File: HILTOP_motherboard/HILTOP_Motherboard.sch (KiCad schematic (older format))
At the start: 216 parts, among them J1 BACKPLANE_PWR, J10 HDMI, J11 DISP_PWR, J12 DISPLAY_PORT, J14 VADJ_B, J15 VADJ_A, J16 SOFT_START_PWR, J17 PWR_LED, J18 USB_B, J19 Micro_SD_Card, J2 ATX_MOLEX_02X12, J20 CAMERA_PORT, J21 EXT_FAN, J22 BACKPLANE_LV_PWR, J23 EXT_FAN, J26 IO_EXP, J27 USB_A, J3 SATA, J4 USB_A_DOUBLE, J5 USB FRONT PANEL, J6 CAN, J7 RS485, J8 EXT_TEMP_MON, J9 RJ45-TRANS_SI-61001-F, U1 LM337BD2TG, U25 STM6719SFWB6F, U39 MCP23017, U42 24LC512

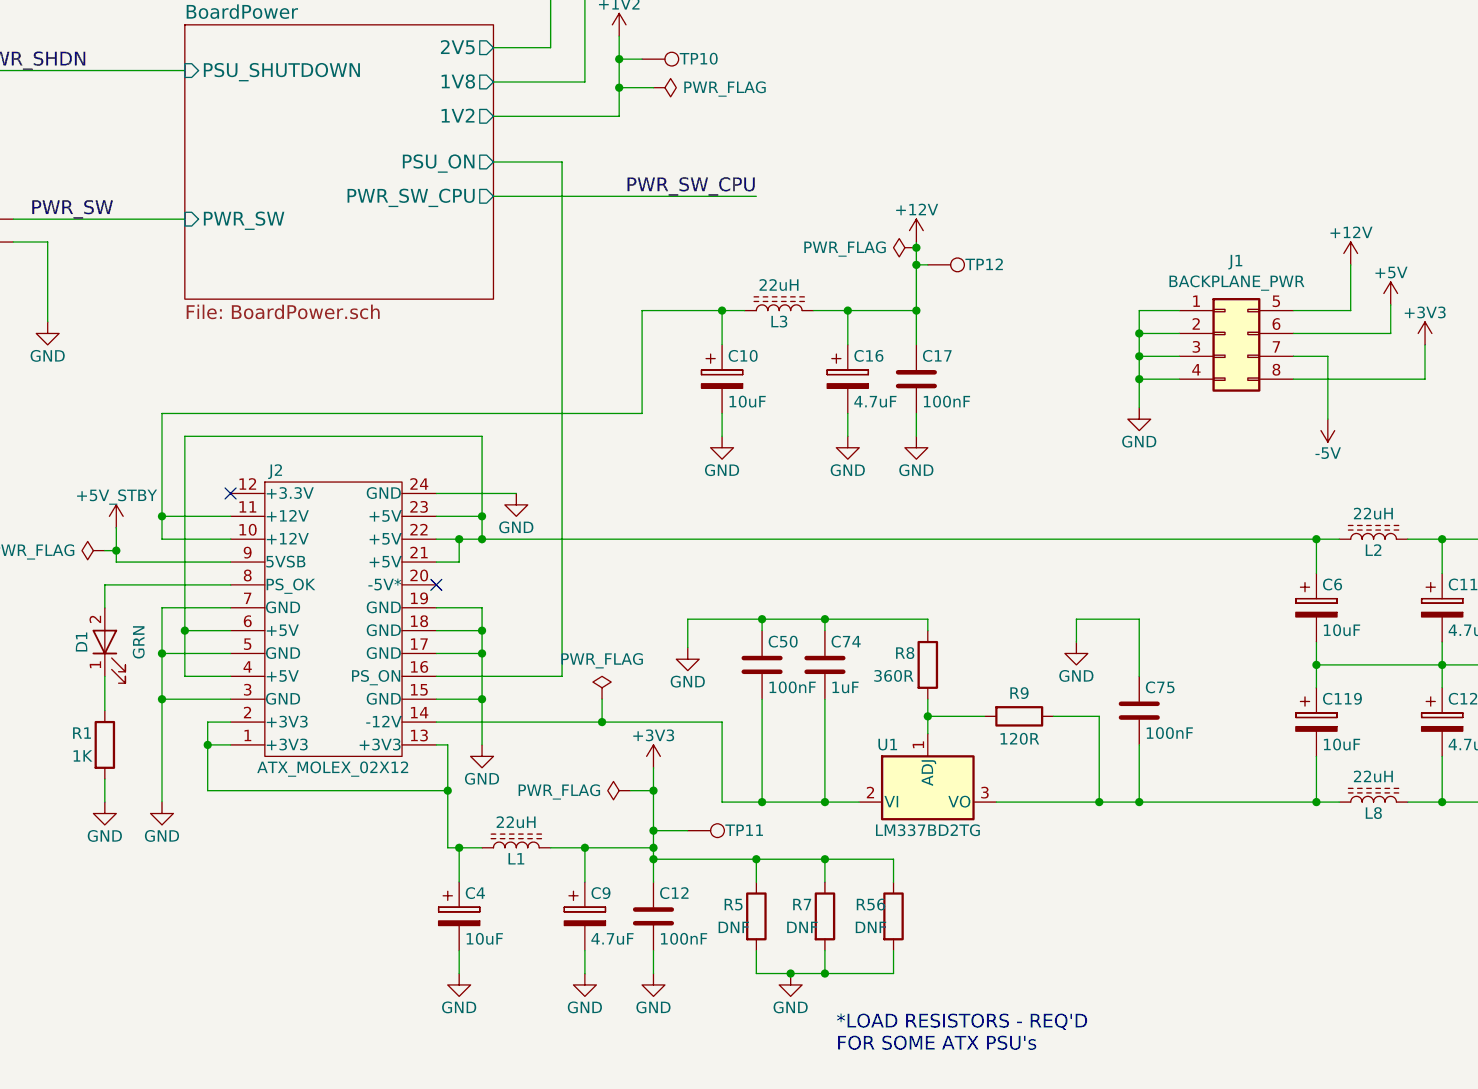
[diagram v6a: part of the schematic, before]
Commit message: Added TVS diodes on PSU inputs, update license details
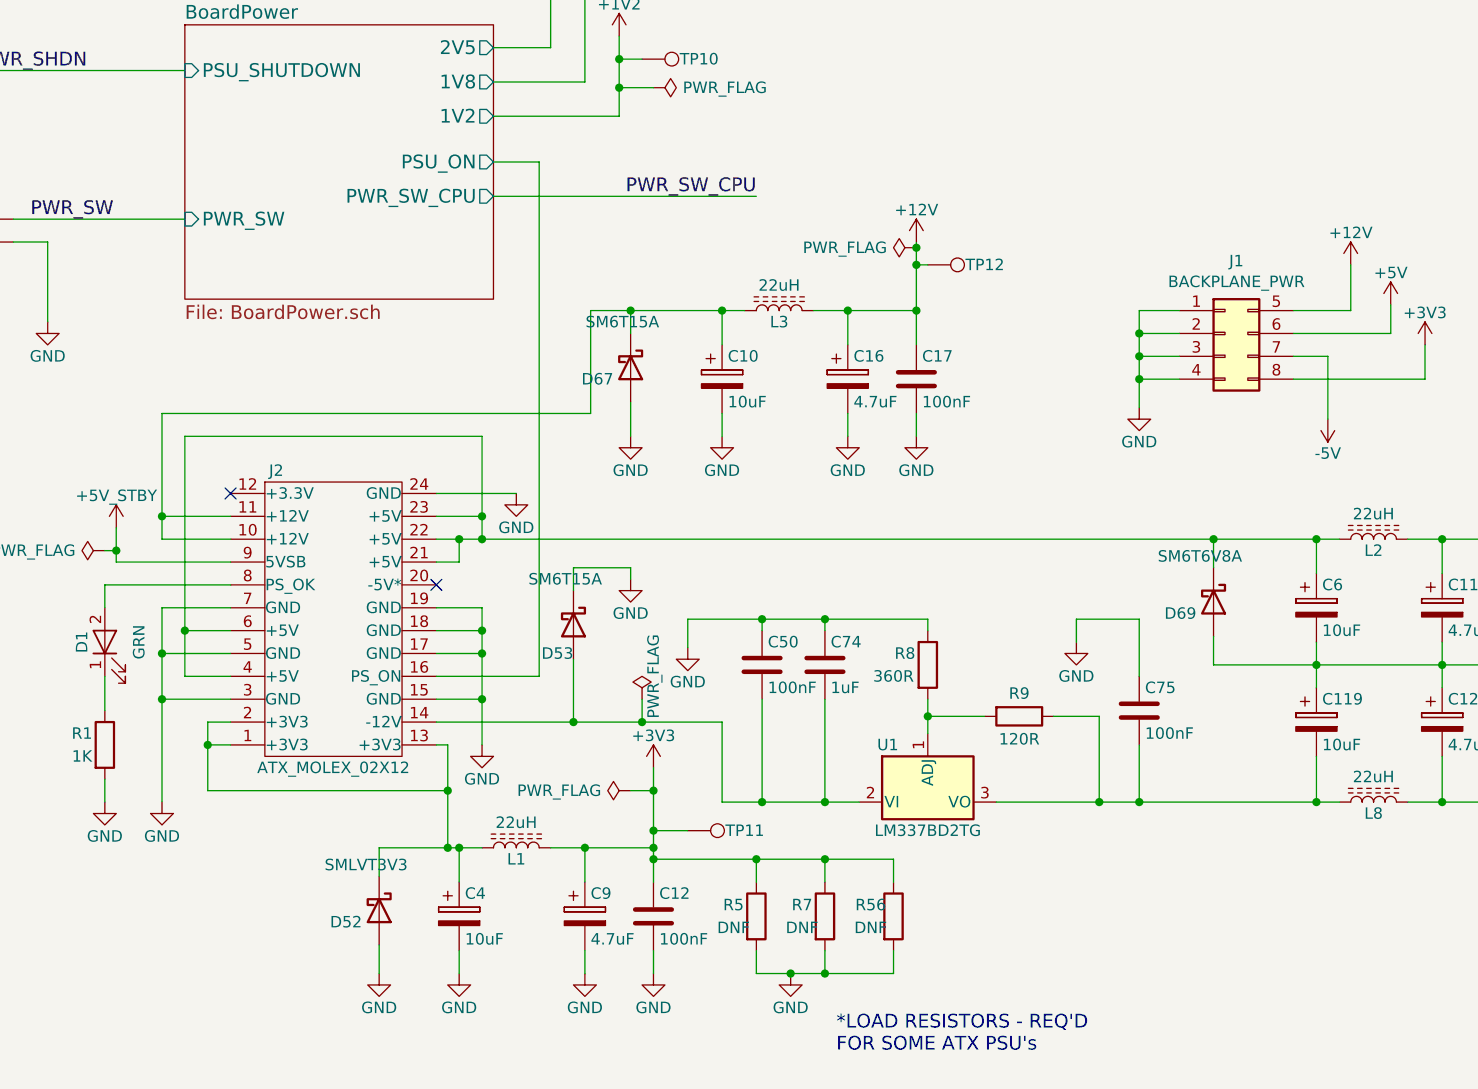
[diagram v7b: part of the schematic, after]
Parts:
- added D52: SMLVT3V3, Diode_SMD:D_SMB, symbol Device:D_Schottky
- added D53, D67: SM6T15A, Diode_SMD:D_SMB, symbol Device:D_Schottky
- added D69: SM6T6V8A, Diode_SMD:D_SMB, symbol Device:D_Schottky
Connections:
- net GND: now also D52.2 (A), D53.1 (K), D67.2 (A), D69.2 (A)
- net at C4.1, J2.1 (+3V3), J2.13 (+3V3)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: now also D52.1 (K)
- net at C6.1, J2.21 (+5V), J2.22 (+5V)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: now also D69.1 (K)
- net at C10.1, J2.10 (+12V), J2.11 (+12V)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: now also D67.1 (K)
- net at C50.2, C74.2, J2.14 (-12V)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: now also D53.2 (A)
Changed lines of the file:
@@
 	1800 13250 1800 13700
 Wire Wire Line
-	3900 13250 1800 13250
+	3675 13250 1800 13250
 Wire Wire Line
-	3900 12800 3900 13250
+	3675 12800 3675 13250
 Wire Wire Line
-	3900 12800 4250 12800
+	3675 12800 3850 12800
 Connection ~ 5100 12800
 Wire Wire Line
@@
 	3800 11600 3800 11700
 Wire Wire Line
-	3550 14400 3000 14400
+	3450 14400 3000 14400
 Wire Wire Line
-	3250 12150 3550 12150
+	3250 12150 3450 12150
 Wire Wire Line
 	1550 14000 2100 14000
@@
 	1    0    0    -1
 $EndComp
-Wire Wire Line
-	3200 13800 6850 13800
 $Comp
 L HILTOP_Motherboard-rescue:R-device R8
@@
 	4250 14950 4250 14600
 Wire Wire Line
-	4250 14600 3725 14600
+	4250 14600 3900 14600
 Wire Wire Line
 	5150 14500 5150 14575
@@
 L power:PWR_FLAG #FLG0129
 U 1 1 5E6340CA
-P 3725 14500
-F 0 "#FLG0129" H 3725 14575 50  0001 C CNN
-F 1 "PWR_FLAG" H 3725 14674 50  0000 C CNN
-F 2 "" H 3725 14500 50  0001 C CNN
-F 3 "" H 3725 14500 50  0001 C CNN
-	1    3725 14500
+P 3900 14500
+F 0 "#FLG0129" H 3900 14575 50  0001 C CNN
+F 1 "PWR_FLAG" V 3950 14600 50  0000 C CNN
+F 2 "" H 3900 14500 50  0001 C CNN
+F 3 "" H 3900 14500 50  0001 C CNN
+	1    3900 14500
 	1    0    0    -1
 $EndComp
 Wire Wire Line
-	3725 14500 3725 14600
-Connection ~ 3725 14600
-Wire Wire Line
-	3725 14600 3000 14600
+	3900 14500 3900 14600
+Connection ~ 3900 14600
 $Comp
 L power:PWR_FLAG #FLG0130
@@
 $EndSheet
 Wire Wire Line
-	3550 12150 3550 14400
-Wire Wire Line
 	3250 12300 4400 12300
 Text Label 4400 12300 2    60   ~ 0
@@
 Wire Wire Line
 	4525 8400 4650 8400
+$Comp
+L Device:D_Schottky D67
+U 1 1 60428387
+P 3850 13050
+F 0 "D67" V 3900 12975 50  0000 R CNN
+F 1 "SM6T15A" V 3650 13175 50  0000 R CNN
+F 2 "Diode_SMD:D_SMB" H 3850 13050 50  0001 C CNN
+F 3 "~" H 3850 13050 50  0001 C CNN
+	1    3850 13050
+	0    1    1    0
+$EndComp
+$Comp
+L power:GND #PWR0473
+U 1 1 6086D8C1
+P 3850 13350
+F 0 "#PWR0473" H 3850 13100 50  0001 C CNN
+F 1 "GND" H 3850 13200 50  0000 C CNN
+F 2 "" H 3850 13350 50  0000 C CNN
+F 3 "" H 3850 13350 50  0000 C CNN
+	1    3850 13350
+	1    0    0    -1
+$EndComp
+Wire Wire Line
+	3850 13200 3850 13350
+Wire Wire Line
+	3850 12900 3850 12800
+Connection ~ 3850 12800
+Wire Wire Line
+	3850 12800 4250 12800
+$Comp
+L Device:D_Schottky D69
+U 1 1 60C90533
+P 6400 14075
+F 0 "D69" V 6450 14000 50  0000 R CNN
+F 1 "SM6T6V8A" V 6200 14200 50  0000 R CNN
+F 2 "Diode_SMD:D_SMB" H 6400 14075 50  0001 C CNN
+F 3 "~" H 6400 14075 50  0001 C CNN
+	1    6400 14075
+	0    1    1    0
+$EndComp
+Wire Wire Line
+	6400 14225 6400 14350
+Wire Wire Line
+	6400 14350 6850 14350
+Wire Wire Line
+	6400 13925 6400 13800
+Connection ~ 6400 13800
+Wire Wire Line
+	6400 13800 6850 13800
+$Comp
+L Device:D_Schottky D53
+U 1 1 60F71958
+P 3600 14175
+F 0 "D53" V 3725 14175 50  0000 R CNN
+F 1 "SM6T15A" V 3400 14300 50  0000 R CNN
+F 2 "Diode_SMD:D_SMB" H 3600 14175 50  0001 C CNN
+F 3 "~" H 3600 14175 50  0001 C CNN
+	1    3600 14175
+	0    1    1    0
+$EndComp
+Wire Wire Line
+	3200 13800 6400 13800
+Wire Wire Line
+	3600 14325 3600 14600
+Wire Wire Line
+	3000 14600 3600 14600
+Connection ~ 3600 14600
+Wire Wire Line
+	3600 14600 3900 14600
+$Comp
+L power:GND #PWR0475
+U 1 1 6167D747
+P 3850 13975
+F 0 "#PWR0475" H 3850 13725 50  0001 C CNN
+F 1 "GND" H 3850 13825 50  0000 C CNN
+F 2 "" H 3850 13975 50  0000 C CNN
+F 3 "" H 3850 13975 50  0000 C CNN
+	1    3850 13975
+	1    0    0    -1
+$EndComp
+Wire Wire Line
+	3850 13975 3850 13925
+Wire Wire Line
+	3850 13925 3600 13925
+Wire Wire Line
+	3600 13925 3600 14025
+$Comp
+L Device:D_Schottky D52
+U 1 1 617EAE20
+P 2750 15425
+F 0 "D52" V 2800 15350 50  0000 R CNN
+F 1 "SMLVT3V3" V 2550 15550 50  0000 R CNN
+F 2 "Diode_SMD:D_SMB" H 2750 15425 50  0001 C CNN
+F 3 "~" H 2750 15425 50  0001 C CNN
+	1    2750 15425
+	0    1    1    0
+$EndComp
+Wire Wire Line
+	2750 15275 2750 15150
+Wire Wire Line
+	2750 15150 3050 15150
+Connection ~ 3050 15150
+$Comp
+L power:GND #PWR0476
+U 1 1 619536F3
+P 2750 15700
+F 0 "#PWR0476" H 2750 15450 50  0001 C CNN
+F 1 "GND" H 2750 15550 50  0000 C CNN
+F 2 "" H 2750 15700 50  0000 C CNN
+F 3 "" H 2750 15700 50  0000 C CNN
+	1    2750 15700
+	1    0    0    -1
+$EndComp
+Wire Wire Line
+	2750 15575 2750 15700
+Wire Wire Line
+	3450 12150 3450 14400
 $EndSCHEMATC

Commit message: changed silkscreen to revD and updated sheet information
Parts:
- D52, D53, D67, D69: symbol Device:D_Schottky -> HILTOP_Motherboard-rescue:D_Schottky-Device
- J10: symbol Devtank:HDMI -> HILTOP_Motherboard-rescue:HDMI-Devtank
- J2: symbol Devtank:ATX_MOLEX_02X12 -> HILTOP_Motherboard-rescue:ATX_MOLEX_02X12-Devtank
- J4: symbol Devtank:USB_A_DOUBLE -> HILTOP_Motherboard-rescue:USB_A_DOUBLE-Devtank
- J9: symbol Devtank:RJ45-TRANS_SI-61001-F -> HILTOP_Motherboard-rescue:RJ45-TRANS_SI-61001-F-Devtank
- U25: symbol Devtank:STM6719SFWB6F -> HILTOP_Motherboard-rescue:STM6719SFWB6F-Devtank
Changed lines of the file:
@@
 Sheet 1 12
 Title "HILTOP Motherboard"
-Date "2020-04-28"
-Rev "Rev C"
+Date "2021-02-17"
+Rev "Rev D"
 Comp "Devtank Ltd"
-Comment1 ""
+Comment1 "Part No: 304-001"
 Comment2 ""
 Comment3 ""
@@
 $EndSheet
 $Comp
-L Devtank:HDMI J10
+L HILTOP_Motherboard-rescue:HDMI-Devtank J10
 U 1 1 58C87774
 P 18000 3550
@@
 EXPANSION PORTS
 $Comp
-L Devtank:+5V_STBY #PWR08
+L HILTOP_Motherboard-rescue:+5V_STBY-Devtank #PWR08
 U 1 1 58D96B73
 P 1600 13750
@@
 $EndComp
 $Comp
-L Devtank:-5V #PWR038
+L HILTOP_Motherboard-rescue:-5V-Devtank #PWR038
 U 1 1 590435F3
 P 7850 15300
@@
 $EndComp
 $Comp
-L Devtank:ATX_MOLEX_02X12 J2
+L HILTOP_Motherboard-rescue:ATX_MOLEX_02X12-Devtank J2
 U 1 1 590366A4
 P 2550 14250
@@
 $EndComp
 $Comp
-L Devtank:STM6719SFWB6F U25
+L HILTOP_Motherboard-rescue:STM6719SFWB6F-Devtank U25
 U 1 1 590CCAE9
 P 2500 1450
@@
 $EndComp
 $Comp
-L Devtank:USB_A_DOUBLE J4
+L HILTOP_Motherboard-rescue:USB_A_DOUBLE-Devtank J4
 U 1 1 59159496
 P 5800 1850
@@
 DC_DC_ENABLE
 $Comp
-L Devtank:RJ45-TRANS_SI-61001-F J9
+L HILTOP_Motherboard-rescue:RJ45-TRANS_SI-61001-F-Devtank J9
 U 1 1 592408CB
 P 9375 2450
@@
 $EndComp
 $Comp
-L Devtank:ADJ_DC #PWR021
+L HILTOP_Motherboard-rescue:ADJ_DC-Devtank #PWR021
 U 1 1 5ABAEAC4
 P 4025 8350
@@
 Z2
 $Comp
-L Devtank:+5V_ISO3 #PWR057
+L HILTOP_Motherboard-rescue:+5V_ISO3-Devtank #PWR057
 U 1 1 5AF0C695
 P 12975 8650
@@
 $EndComp
 $Comp
-L Devtank:+5V_ISO4 #PWR058
+L HILTOP_Motherboard-rescue:+5V_ISO4-Devtank #PWR058
 U 1 1 5AF0CE0B
 P 12975 9050
@@
 $EndComp
 $Comp
-L Devtank:GND_ISO3 #PWR071
+L HILTOP_Motherboard-rescue:GND_ISO3-Devtank #PWR071
 U 1 1 5AF0DCF7
 P 15150 9075
@@
 $EndComp
 $Comp
-L Devtank:GND_ISO4 #PWR072
+L HILTOP_Motherboard-rescue:GND_ISO4-Devtank #PWR072
 U 1 1 5AF0E46D
 P 15150 9475
@@
 $EndComp
 $Comp
-L Devtank:+5V_ISO1 #PWR052
+L HILTOP_Motherboard-rescue:+5V_ISO1-Devtank #PWR052
 U 1 1 5AF652C9
 P 12725 4150
@@
 $EndComp
 $Comp
-L Devtank:+5V_ISO2 #PWR050
+L HILTOP_Motherboard-rescue:+5V_ISO2-Devtank #PWR050
 U 1 1 5AF65A43
 P 12475 4500
@@
 $EndComp
 $Comp
-L Devtank:GND_ISO1 #PWR068
+L HILTOP_Motherboard-rescue:GND_ISO1-Devtank #PWR068
 U 1 1 5AF744C3
 P 14450 4650
@@
 $EndComp
 $Comp
-L Devtank:GND_ISO2 #PWR064
+L HILTOP_Motherboard-rescue:GND_ISO2-Devtank #PWR064
 U 1 1 5AF74C3D
 P 14150 4850
@@
 $EndComp
 $Comp
-L Devtank:-5V #PWR095
+L HILTOP_Motherboard-rescue:-5V-Devtank #PWR095
 U 1 1 5D644CD1
 P 6900 13275
@@
 Connection ~ 14800 14700
 $Comp
-L Devtank:GND_ISO3 #PWR0283
+L HILTOP_Motherboard-rescue:GND_ISO3-Devtank #PWR0283
 U 1 1 5DE9A8F7
 P 12550 9275
@@
 $EndComp
 $Comp
-L Devtank:GND_ISO4 #PWR0286
+L HILTOP_Motherboard-rescue:GND_ISO4-Devtank #PWR0286
 U 1 1 5DE9AAA2
 P 12975 9650
@@
 	4525 8400 4650 8400
 $Comp
-L Device:D_Schottky D67
+L HILTOP_Motherboard-rescue:D_Schottky-Device D67
 U 1 1 60428387
 P 3850 13050
@@
 	3850 12800 4250 12800
 $Comp
-L Device:D_Schottky D69
+L HILTOP_Motherboard-rescue:D_Schottky-Device D69
 U 1 1 60C90533
 P 6400 14075
@@
 	6400 13800 6850 13800
 $Comp
-L Device:D_Schottky D53
+L HILTOP_Motherboard-rescue:D_Schottky-Device D53
 U 1 1 60F71958
 P 3600 14175
@@
 	3600 13925 3600 14025
 $Comp
-L Device:D_Schottky D52
+L HILTOP_Motherboard-rescue:D_Schottky-Device D52
 U 1 1 617EAE20
 P 2750 15425
